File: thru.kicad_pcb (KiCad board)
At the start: 2 copper layers, 33.3 x 12.3 mm, 2 parts, among them J2 Conn_Coaxial, J4 Conn_Coaxial

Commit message: made a southwest microwave launch and put it in the thru
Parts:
- J2, J4: footprint Connector_Coaxial:SMA_Molex_73251-1153_EdgeMount_Horizontal -> southwest-microwave-connectors:southwest-super-SMA-292-04A-12
- moved J4 5.85 mm to (184.0, 125.4)
- moved J2 4.84 mm to (150.1, 125.4)
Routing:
- net GND: vias 120 -> 154
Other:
- board size 33.3 x 12.3 mm -> 33.9 x 12.7 mm

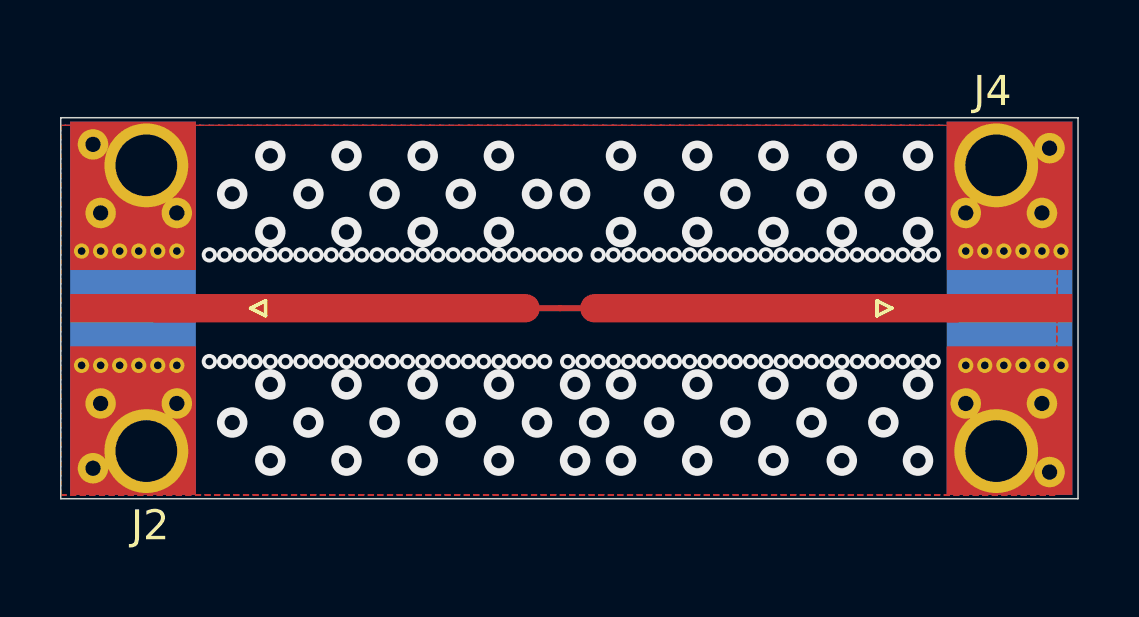
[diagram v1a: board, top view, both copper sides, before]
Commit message: used altium files to build kicad models of mm5800 and started new twpatron
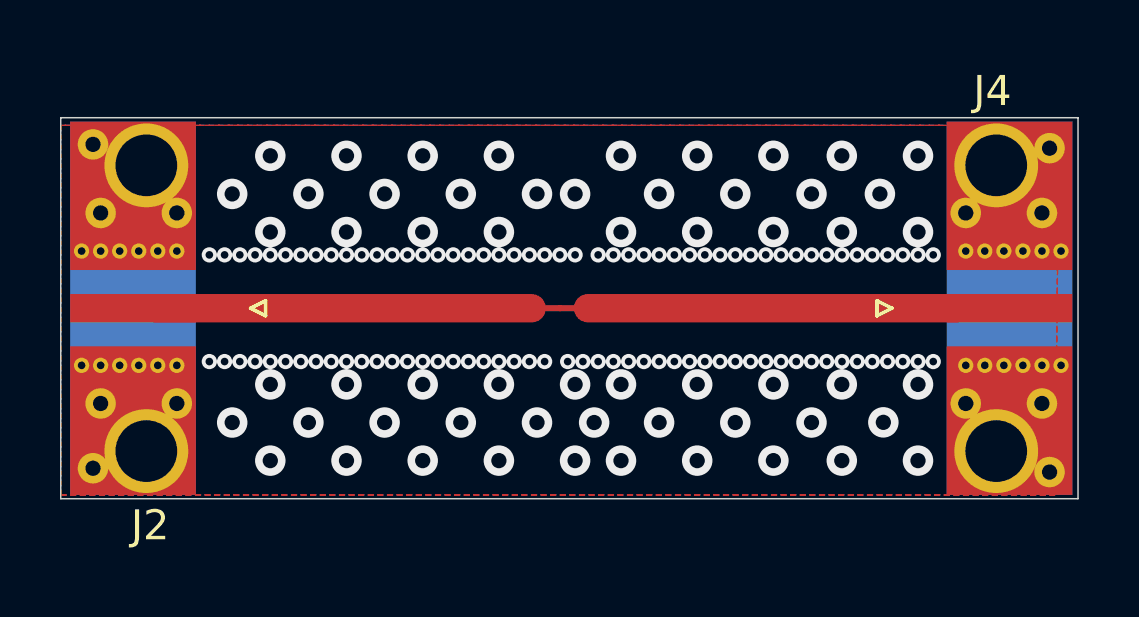
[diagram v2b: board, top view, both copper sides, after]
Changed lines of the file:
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@@
 	)
 	(segment
-		(start 166.641558 125.4)
-		(end 165.494 125.4)
-		(width 0.2)
+		(start 153.175 125.4)
+		(end 165.6972 125.4)
+		(width 0.94742)
 		(layer "F.Cu")
 		(net 2)
@@
 	(segment
 		(start 179.845 125.4)
-		(end 167.786 125.4)
+		(end 167.5768 125.4)
 		(width 0.94742)
 		(layer "F.Cu")
@@
 	(segment
 		(start 166.638442 125.4)
-		(end 167.786 125.4)
+		(end 167.5768 125.4)
 		(width 0.2)
 		(layer "F.Cu")
@@
 	)
 	(segment
-		(start 153.175 125.4)
-		(end 165.494 125.4)
-		(width 0.94742)
+		(start 166.641558 125.4)
+		(end 165.6972 125.4)
+		(width 0.2)
 		(layer "F.Cu")
 		(net 2)
 	)
 	(zone
+		(net 2)
+		(net_name "Net-(J2-In)")
+		(layer "F.Cu")
+		(name "$teardrop_track$")
+		(hatch none 0.1)
+		(priority 30001)
+		(attr
+			(teardrop
+				(type track_end)
+			)
+		)
+		(connect_pads yes
+			(clearance 0)
+		)
+		(min_thickness 0.0254)
+		(filled_areas_thickness no)
+		(fill yes
+			(thermal_gap 0.5)
+			(thermal_bridge_width 0.5)
+			(island_removal_mode 1)
+			(island_area_min 10)
+		)
+		(polygon
+			(pts
+				(xy 166.635518 125.5) (xy 166.635518 125.3) (xy 165.960379 125.006125) (xy 165.6962 125.4) (xy 165.960379 125.793875)
+			)
+		)
+	)
+	(zone
+		(net 2)
+		(net_name "Net-(J2-In)")
+		(layer "F.Cu")
+		(name "$teardrop_track$")
+		(hatch none 0.1)
+		(priority 30000)
+		(attr
+			(teardrop
+				(type track_end)
+			)
+		)
+		(connect_pads yes
+			(clearance 0)
+		)
+		(min_thickness 0.0254)
+		(filled_areas_thickness no)
+		(fill yes
+			(thermal_gap 0.5)
+			(thermal_bridge_width 0.5)
+			(island_removal_mode 1)
+			(island_area_min 10)
+		)
+		(polygon
+			(pts
+				(xy 166.638482 125.3) (xy 166.638482 125.5) (xy 167.313621 125.793875) (xy 167.5778 125.4) (xy 167.313621 125.006125)
+			)
+		)
+	)
+	(zone
